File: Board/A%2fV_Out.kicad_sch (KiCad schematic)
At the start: 28 parts, among them IC2 74245DW, X1 1503_09, X2 D-SUB15-HDR15RA

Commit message: working on r3.1a
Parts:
- added R36: 4k7, micropet_v3:0204V, symbol micropet_v3-eagle-import:R-EU_0204/2V
- added R37: 470, micropet_v3:0204V, symbol micropet_v3-eagle-import:R-EU_0204/2V
- R12: value 3k3 -> 4k7
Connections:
- net GND: now also R37.2
- net TTLSOUND: now also R36.2
- net at C49.1, R12.1, R19.1: no longer C52.1
- new net: C52.1, R36.1, R37.1
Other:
- note added: "3.0B: - add voltage divider to dim beeper volume 3.1A: - add 2nd voltage divider to eliminate channel cross-talk"
- note added: "MICROPET-V3.1A"
- note added: "MICROPET-V3.1A-20241230"
- note removed: "3.0B: - add voltage divider to dim beeper volume"
- note removed: "MICROPET-V3.0B"
- note removed: "MICROPET-V3.0B-20240523"
- moved on the sheet: R19
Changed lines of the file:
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@@
 	(paper "User" 334.823 246.532)
 	(junction
-		(at 133.35 33.02)
+		(at 104.14 33.02)
+		(diameter 0)
+		(color 0 0 0 0)
+	)
+	(junction
+		(at 121.92 40.64)
 		(diameter 0)
 		(color 0 0 0 0)
@@
 	)
 	(junction
-		(at 180.34 134.62)
+		(at 129.54 33.02)
 		(diameter 0)
 		(color 0 0 0 0)
 	)
 	(junction
-		(at 177.8 124.46)
+		(at 180.34 134.62)
 		(diameter 0)
 		(color 0 0 0 0)
 	)
 	(junction
-		(at 121.92 33.02)
+		(at 177.8 124.46)
 		(diameter 0)
 		(color 0 0 0 0)
@@
 	)
 	(junction
+		(at 129.54 73.66)
+		(diameter 0)
+		(color 0 0 0 0)
+	)
+	(junction
 		(at 182.88 139.7)
 		(diameter 0)
@@
 	(wire
 		(pts
-			(xy 121.92 60.96) (xy 121.92 33.02)
+			(xy 129.54 60.96) (xy 129.54 33.02)
 		)
 		(stroke
@@
 	(wire
 		(pts
+			(xy 121.92 71.12) (xy 121.92 73.66)
+		)
+		(stroke
+			(width 0)
+			(type default)
+		)
+	)
+	(wire
+		(pts
 			(xy 78.74 58.42) (xy 93.98 58.42)
 		)
@@
 	(wire
 		(pts
+			(xy 121.92 40.64) (xy 142.24 40.64)
+		)
+		(stroke
+			(width 0)
+			(type default)
+		)
+	)
+	(wire
+		(pts
 			(xy 134.62 137.16) (xy 134.62 132.08)
 		)
@@
 	(wire
 		(pts
-			(xy 119.38 33.02) (xy 121.92 33.02)
+			(xy 119.38 33.02) (xy 129.54 33.02)
 		)
 		(stroke
@@
 	(wire
 		(pts
-			(xy 160.02 73.66) (xy 121.92 73.66)
+			(xy 160.02 73.66) (xy 129.54 73.66)
 		)
 		(stroke
@@
 	(wire
 		(pts
-			(xy 121.92 33.02) (xy 133.35 33.02)
+			(xy 167.64 33.02) (xy 167.64 48.26)
 		)
 		(stroke
-			(width 0)
-			(type default)
+			(width 0.1524)
+			(type solid)
 		)
 	)
 	(wire
 		(pts
-			(xy 167.64 33.02) (xy 167.64 48.26)
+			(xy 109.22 40.64) (xy 104.14 40.64)
 		)
 		(stroke
-			(width 0.1524)
-			(type solid)
+			(width 0)
+			(type default)
 		)
 	)
@@
 	(wire
 		(pts
-			(xy 109.22 109.22) (xy 114.3 109.22)
+			(xy 121.92 40.64) (xy 119.38 40.64)
 		)
 		(stroke
-			(width 0.1524)
-			(type solid)
+			(width 0)
+			(type default)
 		)
 	)
 	(wire
 		(pts
-			(xy 177.8 124.46) (xy 182.88 124.46)
+			(xy 109.22 109.22) (xy 114.3 109.22)
 		)
 		(stroke
@@
 	(wire
 		(pts
-			(xy 142.24 40.64) (xy 133.35 40.64)
+			(xy 177.8 124.46) (xy 182.88 124.46)
 		)
 		(stroke
-			(width 0)
-			(type default)
+			(width 0.1524)
+			(type solid)
 		)
 	)
@@
 	(wire
 		(pts
+			(xy 121.92 40.64) (xy 121.92 60.96)
+		)
+		(stroke
+			(width 0)
+			(type default)
+		)
+	)
+	(wire
+		(pts
 			(xy 76.2 106.68) (xy 60.96 106.68)
 		)
@@
 	(wire
 		(pts
+			(xy 104.14 33.02) (xy 109.22 33.02)
+		)
+		(stroke
+			(width 0.1524)
+			(type solid)
+		)
+	)
+	(wire
+		(pts
 			(xy 134.62 132.08) (xy 139.7 132.08)
 		)
@@
 	(wire
 		(pts
+			(xy 121.92 73.66) (xy 129.54 73.66)
+		)
+		(stroke
+			(width 0)
+			(type default)
+		)
+	)
+	(wire
+		(pts
 			(xy 160.02 73.66) (xy 160.02 71.12)
 		)
@@
 	(wire
 		(pts
-			(xy 134.62 172.72) (xy 162.56 172.72)
+			(xy 104.14 40.64) (xy 104.14 33.02)
 		)
 		(stroke
-			(width 0.1524)
-			(type solid)
+			(width 0)
+			(type default)
 		)
 	)
 	(wire
 		(pts
-			(xy 68.58 157.48) (xy 78.74 157.48)
+			(xy 134.62 172.72) (xy 162.56 172.72)
 		)
 		(stroke
@@
 	(wire
 		(pts
-			(xy 149.86 40.64) (xy 160.02 40.64)
+			(xy 68.58 157.48) (xy 78.74 157.48)
 		)
 		(stroke
@@
 	(wire
 		(pts
-			(xy 121.92 73.66) (xy 121.92 71.12)
+			(xy 149.86 40.64) (xy 160.02 40.64)
 		)
 		(stroke
@@
 	(wire
 		(pts
-			(xy 133.35 40.64) (xy 133.35 33.02)
+			(xy 129.54 73.66) (xy 129.54 71.12)
 		)
 		(stroke
-			(width 0)
-			(type default)
+			(width 0.1524)
+			(type solid)
 		)
 	)
@@
 	(wire
 		(pts
-			(xy 66.04 33.02) (xy 109.22 33.02)
+			(xy 66.04 33.02) (xy 104.14 33.02)
 		)
 		(stroke
@@
 	(wire
 		(pts
-			(xy 133.35 33.02) (xy 142.24 33.02)
+			(xy 129.54 33.02) (xy 142.24 33.02)
 		)
 		(stroke
@@
 		)
 	)
-	(text "3.0B:\n- add voltage divider to dim beeper volume"
+	(text "3.0B:\n- add voltage divider to dim beeper volume\n3.1A:\n- add 2nd voltage divider to eliminate channel cross-talk"
 		(exclude_from_sim no)
-		(at 208.534 183.642 0)
+		(at 52.07 211.582 0)
 		(effects
 			(font
@@
 		)
 	)
-	(text "MICROPET-V3.0B"
+	(text "MICROPET-V3.1A"
 		(exclude_from_sim no)
 		(at 208.28 195.58 0)
@@
 		)
 	)
-	(text "MICROPET-V3.0B-20240523"
+	(text "MICROPET-V3.1A-20241230"
 		(exclude_from_sim no)
 		(at 208.28 218.44 0)
@@
 	(symbol
 		(lib_id "micropet_v3-eagle-import:R-EU_0204/2V")
+		(at 121.92 66.04 270)
+		(unit 1)
+		(exclude_from_sim no)
+		(in_bom yes)
+		(on_board yes)
+		(dnp no)
+		(property "Reference" "R37"
+			(at 123.9266 62.23 0)
+			(effects
+				(font
+					(size 1.778 1.5113)
+				)
+				(justify left bottom)
+			)
+		)
+		(property "Value" "470"
+			(at 118.618 62.23 0)
+			(effects
+				(font
+					(size 1.778 1.5113)
+				)
+				(justify left bottom)
+			)
+		)
+		(property "Footprint" "micropet_v3:0204V"
+			(at 121.92 66.04 0)
+			(effects
+				(font
+					(size 1.27 1.27)
+				)
+				(hide yes)
+			)
+		)
+		(property "Datasheet" ""
+			(at 121.92 66.04 0)
+			(effects
+				(font
+					(size 1.27 1.27)
+				)
+				(hide yes)
+			)
+		)
+		(property "Description" ""
+			(at 121.92 66.04 0)
+			(effects
+				(font
+					(size 1.27 1.27)
+				)
+				(hide yes)
+			)
+		)
+		(pin "1"
+		)
+		(pin "2"
+		)
+		(instances
+			(project "micropet_v3"
+				(path "/d690d13f-2f18-4476-a6d5-736cfe9a0ec3/cc5c915a-c2a7-4cf5-92a1-dac49395dedd"
+					(reference "R37")
+					(unit 1)
+				)
+			)
+		)
+	)
+	(symbol
+		(lib_id "micropet_v3-eagle-import:R-EU_0204/2V")
 		(at 167.64 139.7 0)
 		(unit 1)
@@
 			)
 		)
-		(property "Value" "3k3"
+		(property "Value" "4k7"
 			(at 118.11 29.718 0)
 			(effects
@@
 	)
 	(symbol
+		(lib_id "micropet_v3-eagle-import:R-EU_0204/2V")
+		(at 114.3 40.64 180)
+		(unit 1)
+		(exclude_from_sim no)
+		(in_bom yes)
+		(on_board yes)
+		(dnp no)
+		(property "Reference" "R36"
+			(at 118.11 42.1386 0)
+			(effects
+				(font
+					(size 1.778 1.5113)
+				)
+				(justify left bottom)
+			)
+		)
+		(property "Value" "4k7"
+			(at 118.11 37.338 0)
+			(effects
+				(font
+					(size 1.778 1.5113)
+				)
+				(justify left bottom)
+			)
+		)
+		(property "Footprint" "micropet_v3:0204V"
+			(at 114.3 40.64 0)
+			(effects
+				(font
+					(size 1.27 1.27)
+				)
+				(hide yes)
+			)
+		)
+		(property "Datasheet" ""
+			(at 114.3 40.64 0)
+			(effects
+				(font
+					(size 1.27 1.27)
+				)
+				(hide yes)
+			)
+		)
+		(property "Description" ""
+			(at 114.3 40.64 0)
+			(effects
+				(font
+					(size 1.27 1.27)
+				)
+				(hide yes)
+			)
+		)
+		(pin "1"
+		)
+		(pin "2"
+		)
+		(instances
+			(project "micropet_v3"
+				(path "/d690d13f-2f18-4476-a6d5-736cfe9a0ec3/cc5c915a-c2a7-4cf5-92a1-dac49395dedd"
+					(reference "R36")
+					(unit 1)
+				)
+			)
+		)
+	)
+	(symbol
 		(lib_id "micropet_v3-eagle-import:D-SUB15-HDR15RA")
 		(at 198.12 147.32 0)
@@
 	(symbol
 		(lib_id "micropet_v3-eagle-import:R-EU_0204/2V")
-		(at 121.92 66.04 270)
+		(at 129.54 66.04 270)
 		(unit 1)
 		(exclude_from_sim no)
@@
 		(dnp no)
 		(property "Reference" "R19"
-			(at 123.4186 62.23 0)
+			(at 131.5466 62.23 0)
 			(effects
 				(font
@@
 		)
 		(property "Value" "470"
-			(at 118.618 62.23 0)
+			(at 126.238 62.23 0)
 			(effects
 				(font
@@
 		)
 		(property "Footprint" "micropet_v3:0204V"
-			(at 121.92 66.04 0)
+			(at 129.54 66.04 0)
 			(effects
 				(font
@@
 		)
 		(property "Datasheet" ""
-			(at 121.92 66.04 0)
+			(at 129.54 66.04 0)
 			(effects
 				(font
@@
 		)
 		(property "Description" ""
-			(at 121.92 66.04 0)
+			(at 129.54 66.04 0)
 			(effects
 				(font

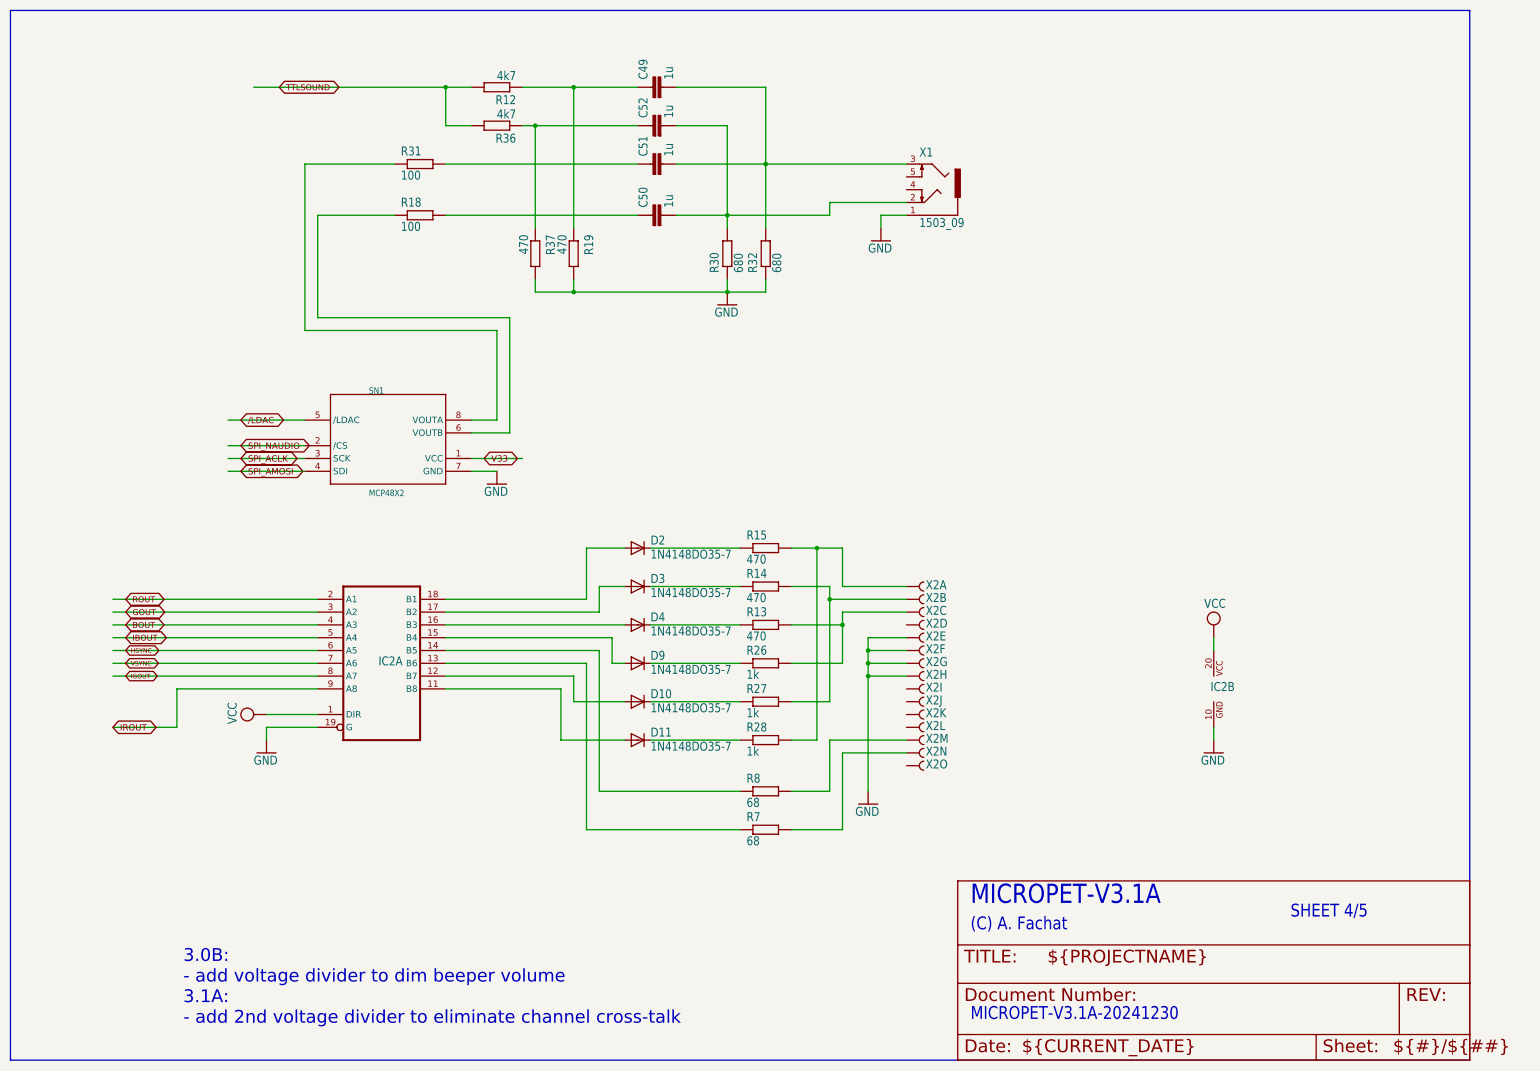
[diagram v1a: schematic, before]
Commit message: adapt audio output caps
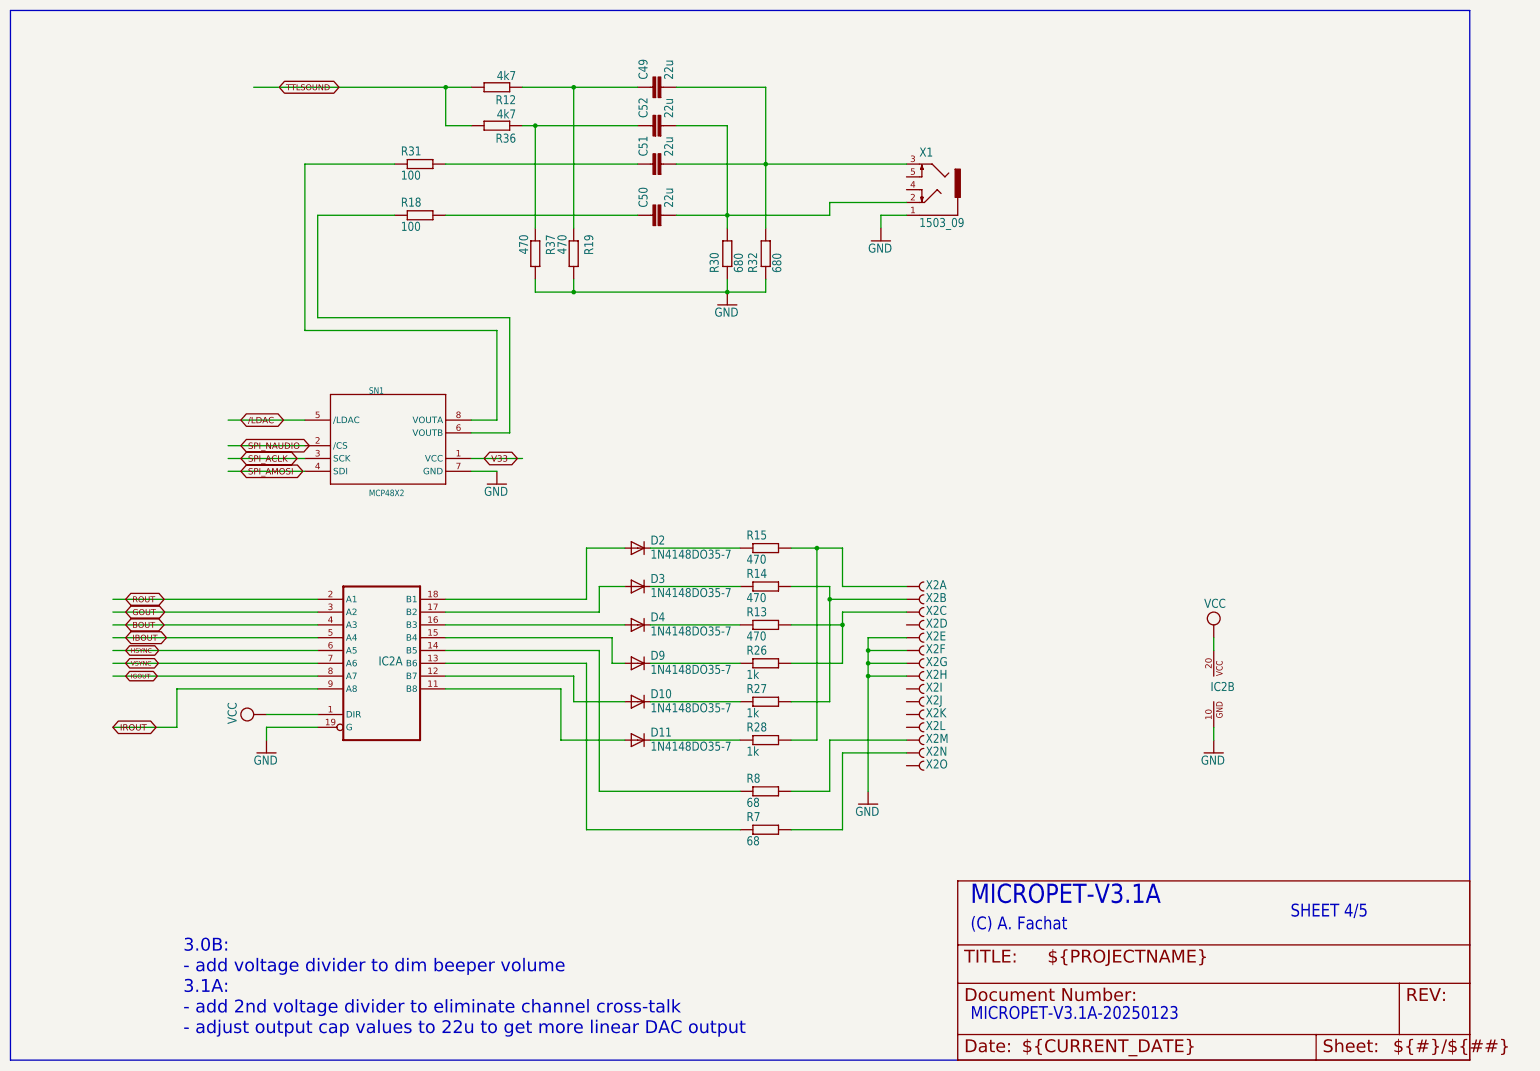
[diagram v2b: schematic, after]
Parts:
- C49, C50, C51, C52: value 1u -> 22u
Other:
- note added: "3.0B: - add voltage divider to dim beeper volume 3.1A: - add 2nd voltage divider to eliminate channel cross-talk - adjust output cap values to 22u to get more linear DAC output"
- note added: "MICROPET-V3.1A-20250123"
- note removed: "3.0B: - add voltage divider to dim beeper volume 3.1A: - add 2nd voltage divider to eliminate channel cross-talk"
- note removed: "MICROPET-V3.1A-20241230"
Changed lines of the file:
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@@
 		)
 	)
-	(text "3.0B:\n- add voltage divider to dim beeper volume\n3.1A:\n- add 2nd voltage divider to eliminate channel cross-talk"
+	(text "3.0B:\n- add voltage divider to dim beeper volume\n3.1A:\n- add 2nd voltage divider to eliminate channel cross-talk\n- adjust output cap values to 22u to get more linear DAC output"
 		(exclude_from_sim no)
 		(at 52.07 211.582 0)
@@
 		)
 	)
-	(text "MICROPET-V3.1A-20241230"
+	(text "MICROPET-V3.1A-20250123"
 		(exclude_from_sim no)
 		(at 208.28 218.44 0)
@@
 			)
 		)
-		(property "Value" "1u"
+		(property "Value" "22u"
 			(at 149.479 46.736 0)
 			(effects
@@
 			)
 		)
-		(property "Value" "1u"
+		(property "Value" "22u"
 			(at 149.479 56.896 0)
 			(effects
@@
 			)
 		)
-		(property "Value" "1u"
+		(property "Value" "22u"
 			(at 149.479 39.116 0)
 			(effects
@@
 			)
 		)
-		(property "Value" "1u"
+		(property "Value" "22u"
 			(at 149.479 31.496 0)
 			(effects
